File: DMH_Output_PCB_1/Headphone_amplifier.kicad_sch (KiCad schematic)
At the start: 24 parts, among them U11 TL074, U12 NE5532, U13 NE5532, U14 NE5532, U15 NE5532

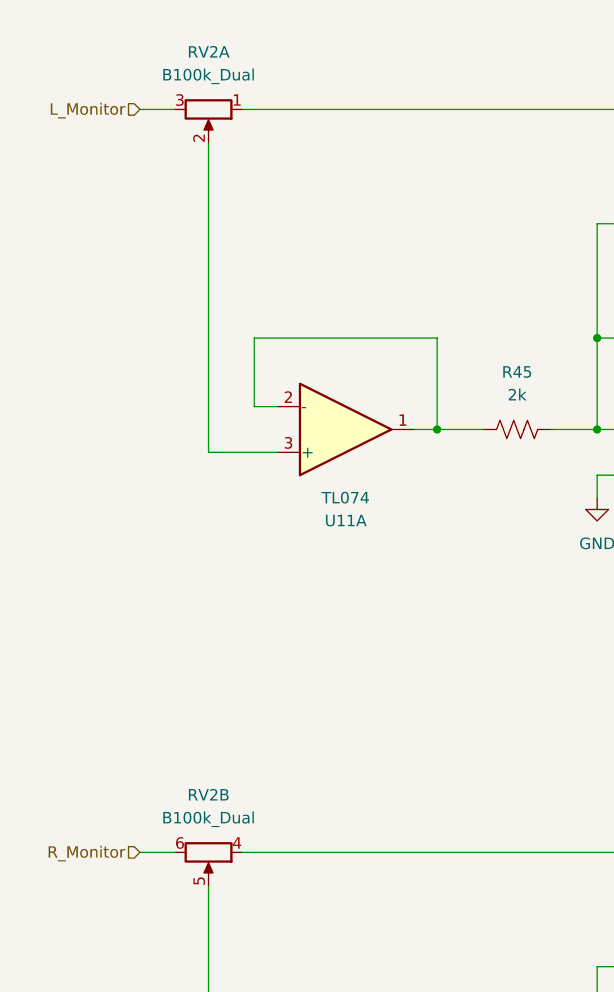
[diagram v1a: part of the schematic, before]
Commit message: Redesigned external input preamp
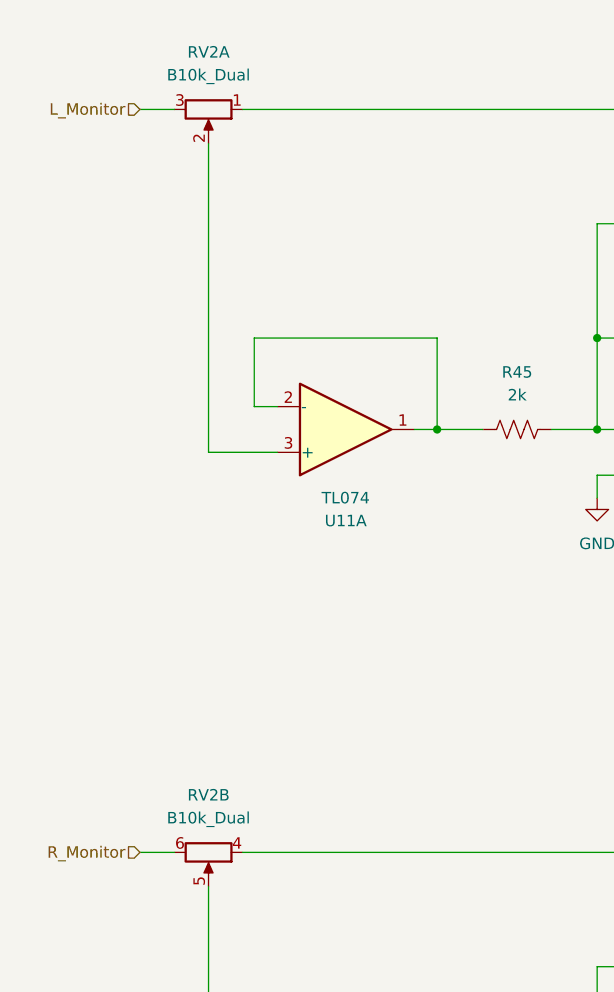
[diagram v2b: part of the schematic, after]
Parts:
- RV2: value B100k_Dual -> B10k_Dual
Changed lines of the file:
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@@
 			)
 		)
-		(property "Value" "B100k_Dual"
+		(property "Value" "B10k_Dual"
 			(at 35.56 104.14 90)
 			(effects
@@
 			)
 		)
-		(property "Value" "B100k_Dual"
+		(property "Value" "B10k_Dual"
 			(at 35.56 21.59 90)
 			(effects

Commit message: Adjusted gains
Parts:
- R45, R47: value 2k -> 1k
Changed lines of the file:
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@@
 			)
 		)
-		(property "Value" "2k"
+		(property "Value" "1k"
 			(at 69.85 57.15 90)
 			(effects
@@
 			)
 		)
-		(property "Value" "2k"
+		(property "Value" "1k"
 			(at 69.85 139.7 90)
 			(effects
@@
 			)
 		)
+		(property "Function" ""
+			(at 69.85 143.51 0)
+			(effects
+				(font
+					(size 1.27 1.27)
+				)
+			)
+		)

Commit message: Updated meters resistor values
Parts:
- U12, U13, U14, U15: footprint (none) -> Package_DIP:DIP-8_W7.62mm_Socket
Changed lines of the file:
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@@
 			)
 		)
-		(property "Footprint" ""
+		(property "Footprint" "Package_DIP:DIP-8_W7.62mm_Socket"
 			(at 152.4 132.08 0)
 			(effects
@@
 			)
 		)
-		(property "Footprint" ""
+		(property "Footprint" "Package_DIP:DIP-8_W7.62mm_Socket"
 			(at 127 66.04 0)
 			(effects
@@
 			)
 		)
-		(property "Footprint" ""
+		(property "Footprint" "Package_DIP:DIP-8_W7.62mm_Socket"
 			(at 152.4 110.49 0)
 			(effects
@@
 			)
 		)
-		(property "Footprint" ""
+		(property "Footprint" "Package_DIP:DIP-8_W7.62mm_Socket"
 			(at 152.4 27.94 0)
 			(effects
@@
 			)
 		)
-		(property "Footprint" ""
+		(property "Footprint" "Package_DIP:DIP-8_W7.62mm_Socket"
 			(at 152.4 49.53 0)
 			(effects
@@
 			)
 		)
-		(property "Footprint" ""
+		(property "Footprint" "Package_DIP:DIP-8_W7.62mm_Socket"
 			(at 127 148.59 0)
 			(effects
@@
 			)
 		)
-		(property "Footprint" ""
+		(property "Footprint" "Package_DIP:DIP-8_W7.62mm_Socket"
 			(at 152.4 161.29 0)
 			(effects
@@
 			)
 		)
-		(property "Footprint" ""
+		(property "Footprint" "Package_DIP:DIP-8_W7.62mm_Socket"
 			(at 152.4 78.74 0)
 			(effects

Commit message: Adjustments during breadboarding
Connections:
- net GND: now also U11.5 (+), U13.3 (+), U15.3 (+); no longer U11.12 (+), U13.5 (+), U15.5 (+)
- net at R56.2, R58.1, U14.3 (+)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: now also U15.1, U15.5 (+); no longer U15.3 (+), U15.7
- net at R48.2, R49.1: now also U13.2 (-); no longer U13.6 (-)
- net at R49.2, R52.1, U12.3 (+)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: now also U13.1, U13.5 (+); no longer U13.3 (+), U13.7
- net at RV2.5: now also U11.12 (+); no longer U11.5 (+)
- net at R56.1, R57.2: now also U15.2 (-); no longer U15.6 (-)
- net at C13.1, R44.1, R45.2: now also U11.6 (-); no longer U11.13 (-)
- net at C13.2, R44.2, R48.1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: now also U11.7; no longer U11.14
- new net: R59.1, U15.6 (-), U15.7
- new net: R47.1, U11.13 (-), U11.14
- new net: R53.1, U13.6 (-), U13.7
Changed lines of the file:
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@@
 		(at 127 66.04 0)
 		(mirror x)
-		(unit 2)
+		(unit 1)
 		(exclude_from_sim no)
 		(in_bom yes)
@@
 			)
 		)
+		(property "Function" ""
+			(at 127 66.04 0)
+			(effects
+				(font
+					(size 1.27 1.27)
+				)
+			)
+		)
 		(pin "2"
 		)
@@
 				(path "/58f4306d-5387-4983-bb08-41a2313fd315/45b3c00a-420e-4349-b096-199706c640d6"
 					(reference "U13")
-					(unit 2)
+					(unit 1)
 				)
 			)
@@
 		(at 50.8 143.51 0)
 		(mirror x)
-		(unit 2)
+		(unit 4)
 		(exclude_from_sim no)
 		(in_bom yes)
@@
 			)
 		)
+		(property "Function" ""
+			(at 50.8 143.51 0)
+			(effects
+				(font
+					(size 1.27 1.27)
+				)
+			)
+		)
 		(pin "7"
 		)
@@
 				(path "/58f4306d-5387-4983-bb08-41a2313fd315/45b3c00a-420e-4349-b096-199706c640d6"
 					(reference "U11")
-					(unit 2)
+					(unit 4)
 				)
 			)
@@
 		(at 127 148.59 0)
 		(mirror x)
-		(unit 2)
+		(unit 1)
 		(exclude_from_sim no)
 		(in_bom yes)
@@
 			)
 		)
+		(property "Function" ""
+			(at 127 148.59 0)
+			(effects
+				(font
+					(size 1.27 1.27)
+				)
+			)
+		)
 		(pin "2"
 		)
@@
 				(path "/58f4306d-5387-4983-bb08-41a2313fd315/45b3c00a-420e-4349-b096-199706c640d6"
 					(reference "U15")
-					(unit 2)
+					(unit 1)
 				)
 			)
@@
 		(lib_id "Amplifier_Operational:NE5532")
 		(at 152.4 161.29 0)
-		(unit 1)
+		(unit 2)
 		(exclude_from_sim no)
 		(in_bom yes)
@@
 			)
 		)
+		(property "Function" ""
+			(at 152.4 161.29 0)
+			(effects
+				(font
+					(size 1.27 1.27)
+				)
+			)
+		)
 		(pin "2"
 		)
@@
 				(path "/58f4306d-5387-4983-bb08-41a2313fd315/45b3c00a-420e-4349-b096-199706c640d6"
 					(reference "U15")
-					(unit 1)
+					(unit 2)
 				)
 			)
@@
 		(at 88.9 63.5 0)
 		(mirror x)
-		(unit 4)
+		(unit 2)
 		(exclude_from_sim no)
 		(in_bom yes)
@@
 			)
 		)
+		(property "Function" ""
+			(at 88.9 63.5 0)
+			(effects
+				(font
+					(size 1.27 1.27)
+				)
+			)
+		)
 		(pin "7"
 		)
@@
 				(path "/58f4306d-5387-4983-bb08-41a2313fd315/45b3c00a-420e-4349-b096-199706c640d6"
 					(reference "U11")
-					(unit 4)
+					(unit 2)
 				)
 			)
@@
 			)
 		)
+		(property "Function" ""
+			(at 50.8 60.96 0)
+			(effects
+				(font
+					(size 1.27 1.27)
+				)
+			)
+		)
 		(pin "7"
 		)
@@
 			)
 		)
+		(property "Function" ""
+			(at 88.9 146.05 0)
+			(effects
+				(font
+					(size 1.27 1.27)
+				)
+			)
+		)
 		(pin "7"
 		)
@@
 		(lib_id "Amplifier_Operational:NE5532")
 		(at 152.4 78.74 0)
-		(unit 1)
+		(unit 2)
 		(exclude_from_sim no)
 		(in_bom yes)
@@
 			)
 		)
+		(property "Function" ""
+			(at 152.4 78.74 0)
+			(effects
+				(font
+					(size 1.27 1.27)
+				)
+			)
+		)
 		(pin "2"
 		)
@@
 				(path "/58f4306d-5387-4983-bb08-41a2313fd315/45b3c00a-420e-4349-b096-199706c640d6"
 					(reference "U13")
-					(unit 1)
-				)
-			)
+					(unit 2)
+				)
+			)
